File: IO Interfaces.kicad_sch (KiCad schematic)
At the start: 63 parts, among them J2 MIDI OUT, J3 MIDI IN, J4 DB25_Socket, J5 DB25_Pins, J6 Keyboard, U10 MC68901, U13 74HCT14D, U14 74HC164, U15 74HC86, U16 TL497A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

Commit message: motherboard: Added more footprints for parts and refined the serial comms section further
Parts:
- added C118, C119: 100n, rhais_rcl:C0603, symbol Device:C_Small
- C36, C37: value 30p -> 50p
- U10: footprint Package_DIP:DIP-48_W15.24mm_Socket -> rhais_package-dip:DIP-48_W15.24mm_Socket; MFR (none) -> Multicomp; MPN (none) -> SPC15558; OC_FARNELL (none) -> 1183623
- U14: footprint (none) -> rhais_package-smd:SO-14_3.9x8.65mm_P1.27mm; MFR (none) -> Nexperia; MPN (none) -> 74HC164D,653; OC_FARNELL (none) -> 1085337
- U7, U8: MFR (none) -> Multicomp; MPN (none) -> SPC15503; OC_FARNELL (none) -> 2678575
- Y3: footprint (none) -> rhais_osc:Crystal_HC49-U_Vertical; symbol Device:Crystal_GND23_Small -> Device:Crystal_Small; MFR (none) -> IQD; MPN (none) -> LFXTAL003044; OC_FARNELL (none) -> 9712704
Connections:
- net +5V: now also C118.1, C119.1
- net GND: now also C118.2, C119.2; no longer Y3.2, Y3.3
- net at C37.1, U10.17 (XTAL1): now also Y3.1; no longer Y3.4
- net at C36.1, U10.18 (XTAL2): now also Y3.2; no longer Y3.1
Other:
- note added: "C = 2(CL - (CI + CP)) C = 2*(30pF - 5pF) C = 50pF"
- moved on the sheet: C36, C37

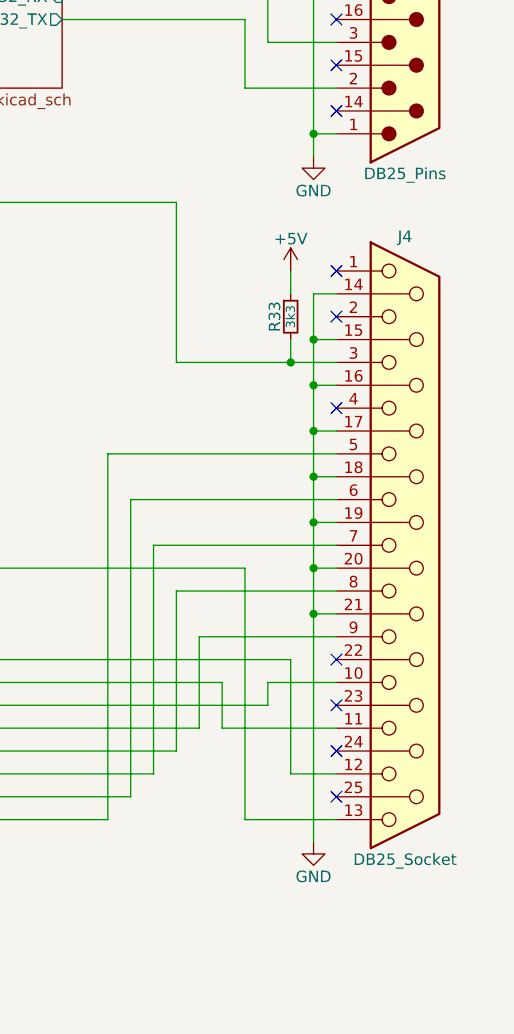
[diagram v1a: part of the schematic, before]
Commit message: motherboard: Corrected the connectors used for the 25-pin interfaces and set their part numbers
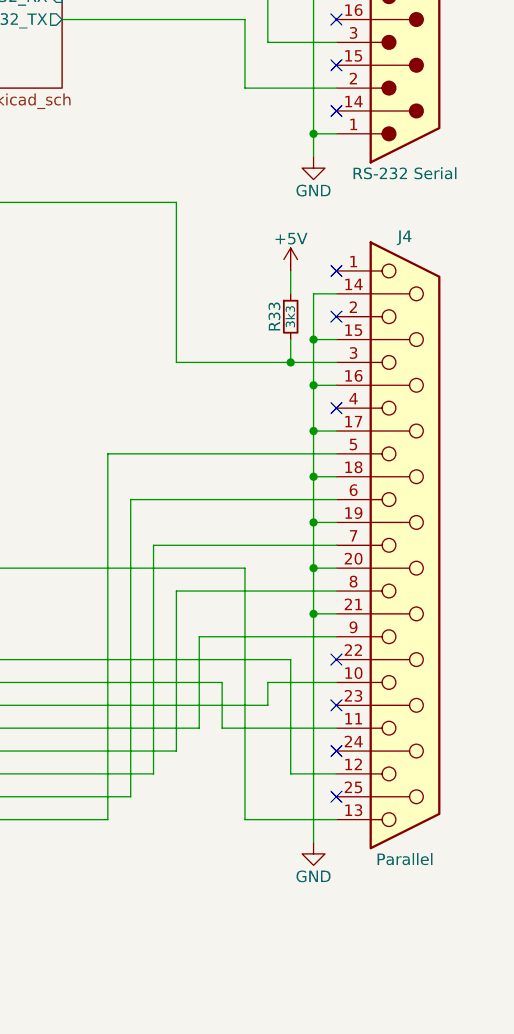
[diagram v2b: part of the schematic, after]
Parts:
- J4: value DB25_Socket -> Parallel; footprint Connector_Dsub:DSUB-25_Socket_Horizontal_P2.77x2.54mm_EdgePinOffset9.40mm -> rhais_connector-dsub:DSUB-25_Socket_Horizontal_P2.77x2.84mm_EdgePinOffset7.70mm_Housed_MountingHolesOffset9.12mm; MFR (none) -> Multicomp; MPN (none) -> 5504F1-25S-02-03-F1; OC_FARNELL (none) -> 1084703
- J5: value DB25_Pins -> RS-232 Serial; footprint Connector_Dsub:DSUB-25_Pins_Horizontal_P2.77x2.54mm_EdgePinOffset9.40mm -> rhais_connector-dsub:DSUB-25_Pins_Horizontal_P2.77x2.84mm_EdgePinOffset7.70mm_Housed_MountingHolesOffset9.12mm; MFR (none) -> Multicomp; MPN (none) -> 5504F1-25P-02-03-F1; OC_FARNELL (none) -> 1084699
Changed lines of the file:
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@@
 			)
 		)
-		(property "Value" "DB25_Pins"
+		(property "Value" "RS-232 Serial"
 			(at 381 149.225 0)
 			(effects
@@
 			)
 		)
-		(property "Footprint" "Connector_Dsub:DSUB-25_Pins_Horizontal_P2.77x2.54mm_EdgePinOffset9.40mm"
+		(property "Footprint" "rhais_connector-dsub:DSUB-25_Pins_Horizontal_P2.77x2.84mm_EdgePinOffset7.70mm_Housed_MountingHolesOffset9.12mm"
 			(at 381 114.3 0)
 			(effects
@@
 			)
 		)
-		(property "Datasheet" "~"
+		(property "Datasheet" "http://www.farnell.com/datasheets/3157360.pdf"
 			(at 381 114.3 0)
 			(effects
@@
 			)
 		)
-		(property "MFR" ""
+		(property "MFR" "Multicomp"
 			(at 381 114.3 0)
 			(effects
@@
 			)
 		)
-		(property "MPN" ""
+		(property "MPN" "5504F1-25P-02-03-F1"
 			(at 381 114.3 0)
 			(effects
@@
 			)
 		)
-		(property "OC_FARNELL" ""
+		(property "OC_FARNELL" "1084699"
 			(at 381 114.3 0)
 			(effects
@@
 			)
 		)
-		(property "Value" "DB25_Socket"
+		(property "Value" "Parallel"
 			(at 381 225.425 0)
 			(effects
@@
 			)
 		)
-		(property "Footprint" "Connector_Dsub:DSUB-25_Socket_Horizontal_P2.77x2.54mm_EdgePinOffset9.40mm"
+		(property "Footprint" "rhais_connector-dsub:DSUB-25_Socket_Horizontal_P2.77x2.84mm_EdgePinOffset7.70mm_Housed_MountingHolesOffset9.12mm"
 			(at 381 190.5 0)
 			(effects
@@
 			)
 		)
-		(property "Datasheet" "~"
+		(property "Datasheet" "http://www.farnell.com/datasheets/4291160.pdf"
 			(at 381 190.5 0)
 			(effects
@@
 			)
 		)
-		(property "MFR" ""
+		(property "MFR" "Multicomp"
 			(at 381 190.5 0)
 			(effects
@@
 			)
 		)
-		(property "MPN" ""
+		(property "MPN" "5504F1-25S-02-03-F1"
 			(at 381 190.5 0)
 			(effects
@@
 			)
 		)
-		(property "OC_FARNELL" ""
+		(property "OC_FARNELL" "1084703"
 			(at 381 190.5 0)
 			(effects

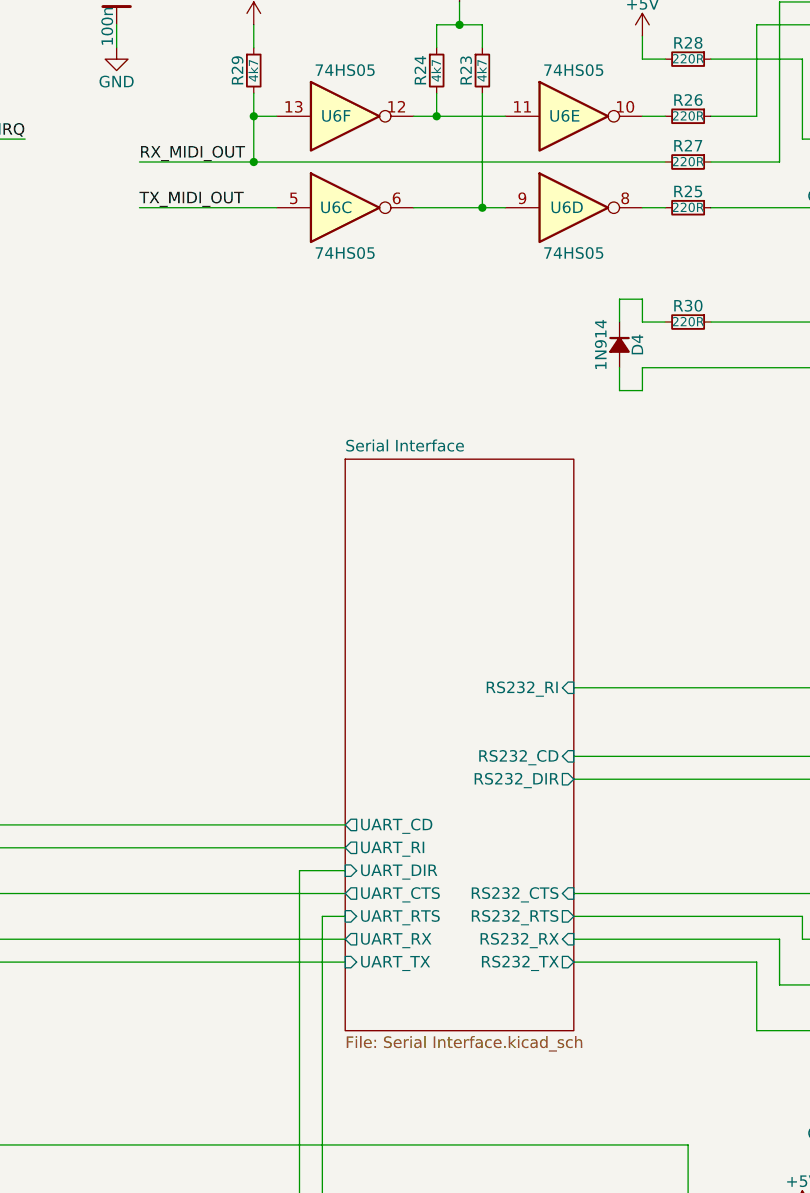
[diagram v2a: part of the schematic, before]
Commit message: motherboard: Completed the MIDI in interface having identified the component PC-900 from the original schematic
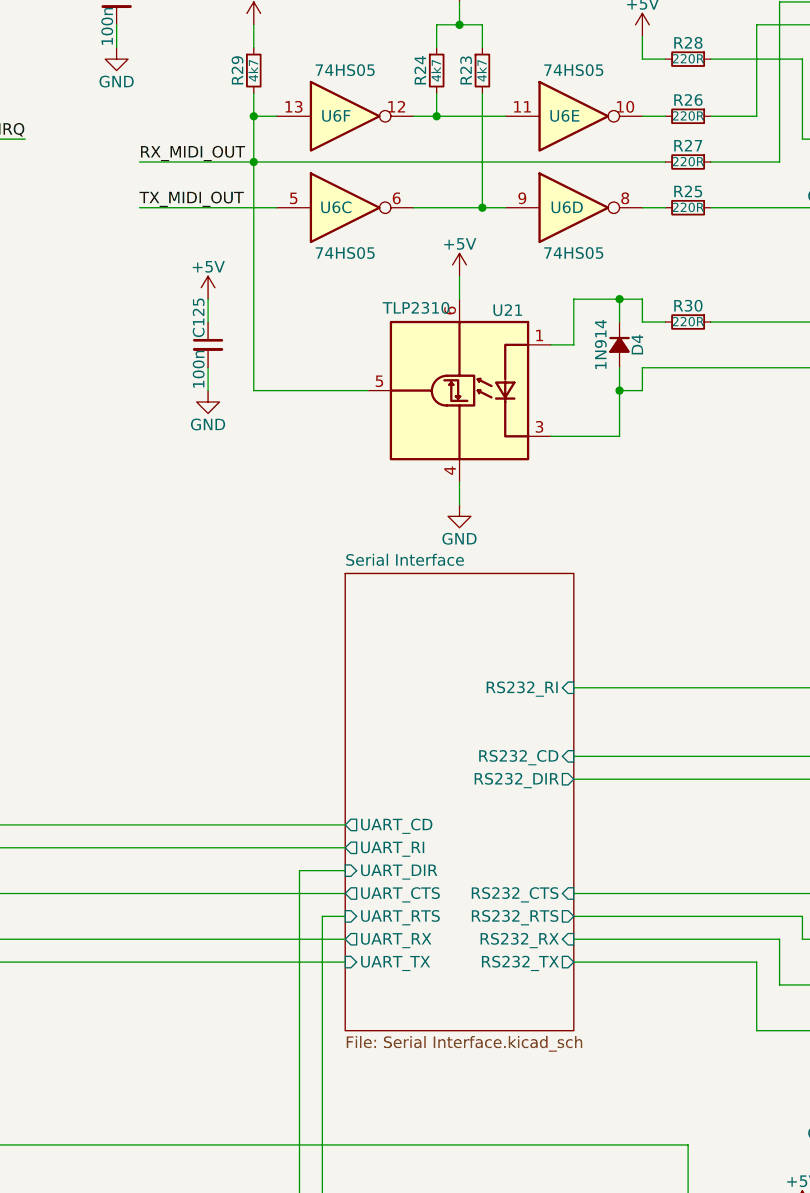
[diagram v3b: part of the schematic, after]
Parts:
- added C125: 100n, rhais_rcl:C0603, symbol Device:C_Small
- added U21: TLP2310, Package_SO:SO-5-6_4.55x3.7mm_P1.27mm, symbol Isolator:TLP2310
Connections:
- net +5V: now also C125.1, U21.6 (VDD)
- net GND: now also C125.2, U21.4 (GND)
- net RX_MIDI_OUT: now also U21.5 (VO)
- net at D4.1 (K), R30.2: now also U21.1 (A)
- net at D4.2 (A), J3.5: now also U21.3 (K)

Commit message: motherboard: Sorted out all the 1N914's having found a suitable part
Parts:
- D4, D5, D6, D7: footprint (none) -> Diode_SMD:D_SOD-323F; MFR (none) -> Onsemi; MPN (none) -> 1N914BWS; OC_FARNELL (none) -> 2453274
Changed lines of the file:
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@@
 			)
 		)
-		(property "Footprint" ""
+		(property "Footprint" "Diode_SMD:D_SOD-323F"
 			(at 88.9 40.64 90)
 			(effects
@@
 			)
 		)
-		(property "Datasheet" "~"
+		(property "Datasheet" "https://www.onsemi.com/download/data-sheet/pdf/1n4148ws-d.pdf"
 			(at 88.9 40.64 90)
 			(effects
@@
 			)
 		)
-		(property "MFR" ""
+		(property "MFR" "Onsemi"
 			(at 88.9 40.64 0)
 			(effects
@@
 			)
 		)
-		(property "MPN" ""
+		(property "MPN" "1N914BWS"
 			(at 88.9 40.64 0)
 			(effects
@@
 			)
 		)
-		(property "OC_FARNELL" ""
+		(property "OC_FARNELL" "2453274"
 			(at 88.9 40.64 0)
 			(effects
@@
 			)
 		)
-		(property "Footprint" ""
+		(property "Footprint" "Diode_SMD:D_SOD-323F"
 			(at 83.82 116.84 90)
 			(effects
@@
 			)
 		)
-		(property "Datasheet" "~"
+		(property "Datasheet" "https://www.onsemi.com/download/data-sheet/pdf/1n4148ws-d.pdf"
 			(at 83.82 116.84 90)
 			(effects
@@
 			)
 		)
-		(property "MFR" ""
+		(property "MFR" "Onsemi"
 			(at 83.82 116.84 0)
 			(effects
@@
 			)
 		)
-		(property "MPN" ""
+		(property "MPN" "1N914BWS"
 			(at 83.82 116.84 0)
 			(effects
@@
 			)
 		)
-		(property "OC_FARNELL" ""
+		(property "OC_FARNELL" "2453274"
 			(at 83.82 116.84 0)
 			(effects
@@
 			)
 		)
-		(property "Footprint" ""
+		(property "Footprint" "Diode_SMD:D_SOD-323F"
 			(at 347.98 63.5 90)
 			(effects
@@
 			)
 		)
-		(property "Datasheet" "~"
+		(property "Datasheet" "https://www.onsemi.com/download/data-sheet/pdf/1n4148ws-d.pdf"
 			(at 347.98 63.5 90)
 			(effects
@@
 			)
 		)
-		(property "MFR" ""
+		(property "MFR" "Onsemi"
 			(at 347.98 63.5 0)
 			(effects
@@
 			)
 		)
-		(property "MPN" ""
+		(property "MPN" "1N914BWS"
 			(at 347.98 63.5 0)
 			(effects
@@
 			)
 		)
-		(property "OC_FARNELL" ""
+		(property "OC_FARNELL" "2453274"
 			(at 347.98 63.5 0)
 			(effects
@@
 			)
 		)
-		(property "Footprint" ""
+		(property "Footprint" "Diode_SMD:D_SOD-323F"
 			(at 96.52 35.56 90)
 			(effects
@@
 			)
 		)
-		(property "Datasheet" "~"
+		(property "Datasheet" "https://www.onsemi.com/download/data-sheet/pdf/1n4148ws-d.pdf"
 			(at 96.52 35.56 90)
 			(effects
@@
 			)
 		)
-		(property "MFR" ""
+		(property "MFR" "Onsemi"
 			(at 96.52 35.56 0)
 			(effects
@@
 			)
 		)
-		(property "MPN" ""
+		(property "MPN" "1N914BWS"
 			(at 96.52 35.56 0)
 			(effects
@@
 			)
 		)
-		(property "OC_FARNELL" ""
+		(property "OC_FARNELL" "2453274"
 			(at 96.52 35.56 0)
 			(effects

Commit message: motherboard: Routed in the sound DMA output and microwire control from SHIFTER
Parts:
- removed unit 1 of U13
- added unit 2 of U13
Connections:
- net ~{SND_INT}: now also U13.3
- net at U14.1 (DSA), U14.2 (DSB), U14.9 (~{MR})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: now also U13.4
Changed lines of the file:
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@@
 	)
 	(symbol
-		(lib_id "74xx:74LS04")
-		(at 101.6 254 0)
-		(unit 1)
-		(exclude_from_sim no)
-		(in_bom yes)
-		(on_board yes)
-		(dnp no)
-		(property "Reference" "U13"
-			(at 100.584 254 0)
-			(effects
-				(font
-					(size 1.27 1.27)
-				)
-			)
-		)
-		(property "Value" "74HCT14D"
-			(at 101.854 248.92 0)
-			(effects
-				(font
-					(size 1.27 1.27)
-				)
-			)
-		)
-		(property "Footprint" "rhais_package-smd:SO-14_3.9x8.65mm_P1.27mm"
-			(at 101.6 254 0)
-			(effects
-				(font
-					(size 1.27 1.27)
-				)
-				(hide yes)
-			)
-		)
-		(property "Datasheet" "https://assets.nexperia.com/documents/data-sheet/74HC_HCT14.pdf"
-			(at 101.6 254 0)
-			(effects
-				(font
-					(size 1.27 1.27)
-				)
-				(hide yes)
-			)
-		)
-		(property "Description" "Hex Inverter"
-			(at 101.6 254 0)
-			(effects
-				(font
-					(size 1.27 1.27)
-				)
-				(hide yes)
-			)
-		)
-		(property "MFR" "Nexperia"
-			(at 101.6 254 0)
-			(effects
-				(font
-					(size 1.27 1.27)
-				)
-				(hide yes)
-			)
-		)
-		(property "MPN" "74HCT14D,653"
-			(at 101.6 254 0)
-			(effects
-				(font
-					(size 1.27 1.27)
-				)
-				(hide yes)
-			)
-		)
-		(property "OC_FARNELL" "1201304"
-			(at 101.6 254 0)
-			(effects
-				(font
-					(size 1.27 1.27)
-				)
-				(hide yes)
-			)
-		)
-		(pin "12"
-		)
-		(pin "10"
-		)
-		(pin "11"
-		)
-		(pin "8"
-		)
-		(pin "7"
-		)
-		(pin "13"
-		)
-		(pin "14"
-		)
-		(pin "4"
-		)
-		(pin "9"
-		)
-		(pin "2"
-		)
-		(pin "6"
-		)
-		(pin "3"
-		)
-		(pin "5"
-		)
-		(pin "1"
-		)
-		(instances
-			(project ""
-				(path "/6cc81c6b-09a2-4492-8ca2-d80a5c796e77/da41d90d-77d6-4e05-9bf5-75a4a2738ae8"
-					(reference "U13")
-					(unit 1)
-				)
-			)
-		)
-	)
-	(symbol
 		(lib_id "power:GND")
 		(at 91.44 134.62 0)
@@
 				)
 			)
+		)
+	)
+	(symbol
+		(lib_id "74xx:74LS04")
+		(at 101.6 254 0)
+		(unit 2)
+		(exclude_from_sim no)
+		(in_bom yes)
+		(on_board yes)
+		(dnp no)
+		(property "Reference" "U13"
+			(at 100.584 254 0)
+			(effects
+				(font
+					(size 1.27 1.27)
+				)
+			)
+		)
+		(property "Value" "74HCT14D"
+			(at 101.6 248.92 0)
+			(effects
+				(font
+					(size 1.27 1.27)
+				)
+			)
+		)
+		(property "Footprint" "rhais_package-smd:SO-14_3.9x8.65mm_P1.27mm"
+			(at 101.6 254 0)
+			(effects
+				(font
+					(size 1.27 1.27)
+				)
+				(hide yes)
+			)
+		)
+		(property "Datasheet" "https://assets.nexperia.com/documents/data-sheet/74HC_HCT14.pdf"
+			(at 101.6 254 0)
+			(effects
+				(font
+					(size 1.27 1.27)
+				)
+				(hide yes)
+			)
+		)
+		(property "Description" "Hex Inverter"
+			(at 101.6 254 0)
+			(effects
+				(font
+					(size 1.27 1.27)
+				)
+				(hide yes)
+			)
+		)
+		(property "MFR" "Nexperia"
+			(at 101.6 254 0)
+			(effects
+				(font
+					(size 1.27 1.27)
+				)
+				(hide yes)
+			)
+		)
+		(property "MPN" "74HCT14D,653"
+			(at 101.6 254 0)
+			(effects
+				(font
+					(size 1.27 1.27)
+				)
+				(hide yes)
+			)
+		)
+		(property "OC_FARNELL" "1201304"
+			(at 101.6 254 0)
+			(effects
+				(font
+					(size 1.27 1.27)
+				)
+				(hide yes)
+			)
+		)
+		(pin "12"
+		)
+		(pin "10"
+		)
+		(pin "11"
+		)
+		(pin "8"
+		)
+		(pin "7"
+		)
+		(pin "13"
+		)
+		(pin "14"
+		)
+		(pin "4"
+		)
+		(pin "9"
+		)
+		(pin "2"
+		)
+		(pin "6"
+		)
+		(pin "3"
+		)
+		(pin "5"
+		)
+		(pin "1"
+		)
+		(instances
+			(project "dragonSTe"
+				(path "/6cc81c6b-09a2-4492-8ca2-d80a5c796e77/da41d90d-77d6-4e05-9bf5-75a4a2738ae8"
+					(reference "U13")
+					(unit 2)
+				)
+			)
